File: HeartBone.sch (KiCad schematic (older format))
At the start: 42 parts, among them J1 CONN_01X05, J2 CONN_01X01, J3 CONN_01X01, J4 USB_B_Micro, SW1 PTS810_SJK_250_SMTR_LFS, SW2 PTS810_SJK_250_SMTR_LFS, SW3 SW_SPDT, U1 25LC1024T-I/SM, U2 Schmitt_Inverter_Single, U3 PIC32MX250F128B-I/SS, U4 TLV76033DBZR, U5 MCP73831-2-OT, Y1 ECS-080-18-23G-JGN-TR

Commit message: dusted off BOM
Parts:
- BT1: value Battery_Cell -> S2B-PH-SM4-TB(LF)(SN)
- D2, D3: value DIODE -> CDBU0130L
- DIS1: value SharpMem_LCD_96x96 -> 505110-1092
- J4: value USB_B_Micro -> 10118193-0001LF
- SW3: value SW_SPDT -> SSSS810701
- U2: value Schmitt_Inverter_Single -> TC7S14FU,LF
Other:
- note added: "MOLEX\n"
- note removed: "MOLEX 505110-1092\n\n"
- note removed: "SPECIFY DIODE PART NUMBER"
- note removed: "TOSHIBA TC7S14FU,LF"
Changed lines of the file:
@@
 P 8500 4050
 F 0 "DIS1" H 8850 2650 60  0000 C CNN
-F 1 "SharpMem_LCD_96x96" H 9200 3950 60  0000 C CNN
+F 1 "505110-1092" H 9000 3950 60  0000 C CNN
 F 2 "Solutions:MOLEX_505110-1092" H 8500 4050 60  0001 C CNN
 F 3 "" H 8500 4050 60  0000 C CNN
@@
 	1    0    0    -1
 $EndComp
-Text Notes 8550 2650 0    60   ~ 0
-TOSHIBA TC7S14FU,LF
 Text Notes 8650 4050 0    60   ~ 0
 Sharp has gone EOL :(
@@
 	1    0    0    -1
 $EndComp
-Text Notes 8450 5700 0    60   ~ 0
-MOLEX 505110-1092\n\n
+Text Notes 9250 4350 0    60   ~ 0
+MOLEX\n
 $Comp
 L Device:R R4
@@
 P 8650 2350
 F 0 "U2" H 8250 2150 60  0000 C CNN
-F 1 "Schmitt_Inverter_Single" H 9200 2250 60  0000 C CNN
+F 1 "TC7S14FU,LF" H 9200 2250 60  0000 C CNN
 F 2 "Solutions:SSOP-5-0.65_PITCH" H 8650 2350 60  0001 C CNN
 F 3 "" H 8650 2350 60  0000 C CNN
@@
 P 1200 1600
 F 0 "J4" H 1255 2067 50  0000 C CNN
-F 1 "USB_B_Micro" H 1255 1976 50  0000 C CNN
+F 1 "10118193-0001LF" H 1255 1976 50  0000 C CNN
 F 2 "Solutions:10118193_microUSB" H 1350 1550 50  0001 C CNN
 F 3 "~" H 1350 1550 50  0001 C CNN
@@
 P 4100 1950
 F 0 "BT1" H 4218 2046 50  0000 L CNN
-F 1 "Battery_Cell" H 4218 1955 50  0000 L CNN
+F 1 "S2B-PH-SM4-TB(LF)(SN)" H 3900 1750 50  0000 L CNN
 F 2 "Solutions:4UCON-0217-20519" V 4100 2010 50  0001 C CNN
 F 3 "~" V 4100 2010 50  0001 C CNN
@@
 U 1 1 5CE86E84
 P 5050 1950
-F 0 "C8" H 4900 2050 50  0000 L CNN
-F 1 "1uF" H 4850 1850 50  0000 L CNN
+F 0 "C8" H 5100 2050 50  0000 L CNN
+F 1 "1uF" H 5100 1850 50  0000 L CNN
 F 2 "Capacitors_SMD:C_0603" H 5050 1950 50  0001 C CNN
 F 3 "" H 5050 1950 50  0000 C CNN
@@
 P 4050 1400
 F 0 "D2" H 3900 1350 50  0000 C CNN
-F 1 "DIODE" H 4050 1275 50  0000 C CNN
+F 1 "CDBU0130L" H 4050 1275 50  0000 C CNN
 F 2 "Diodes_SMD:D_0603" H 4050 1400 50  0001 C CNN
 F 3 "~" H 4050 1400 50  0001 C CNN
@@
 P 4600 1700
 F 0 "D3" H 4450 1650 50  0000 C CNN
-F 1 "DIODE" H 4600 1575 50  0000 C CNN
+F 1 "CDBU0130L" H 4600 1575 50  0000 C CNN
 F 2 "Diodes_SMD:D_0603" H 4600 1700 50  0001 C CNN
 F 3 "~" H 4600 1700 50  0001 C CNN
@@
 	4450 1700 4100 1700
 Connection ~ 4100 1700
-Text Notes 3700 1200 0    50   ~ 0
-SPECIFY DIODE PART NUMBER
 Text Notes 2750 6700 0    50   ~ 0
 2mm MAX HEIGHT
@@
 P 6600 1700
 F 0 "SW3" H 6600 1375 50  0000 C CNN
-F 1 "SW_SPDT" H 6600 1466 50  0000 C CNN
+F 1 "SSSS810701" H 6600 1466 50  0000 C CNN
 F 2 "Solutions:SSSS810701_ALPS_SPDT" H 6600 1700 50  0001 C CNN
 F 3 "" H 6600 1700 50  0001 C CNN

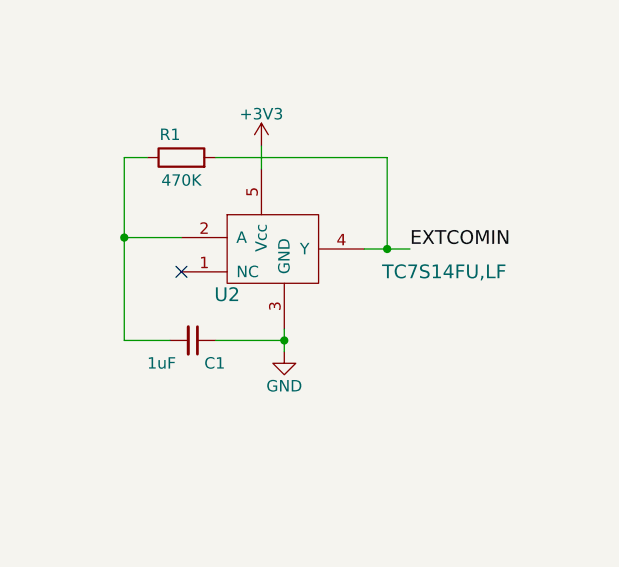
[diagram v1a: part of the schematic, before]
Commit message: UPDATED INVERTER PART NUMBER
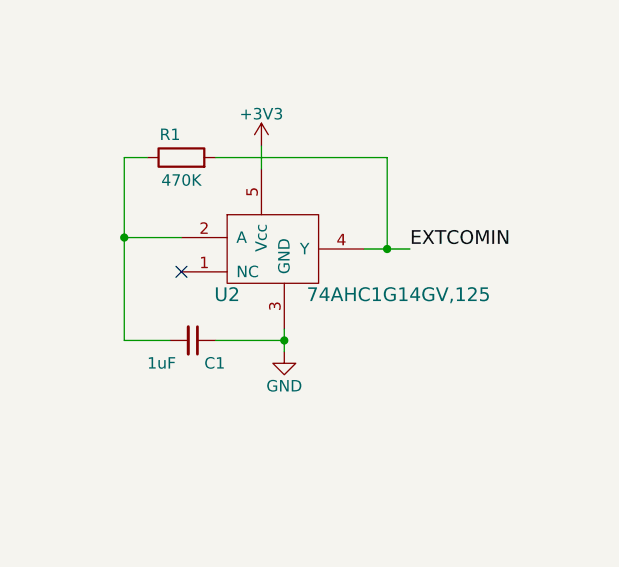
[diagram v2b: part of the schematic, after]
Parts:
- U2: value TC7S14FU,LF -> 74AHC1G14GV,125
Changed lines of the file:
@@
 EESchema Schematic File Version 4
+LIBS:HeartBone-cache
 EELAYER 26 0
 EELAYER END
@@
 P 8650 2350
 F 0 "U2" H 8250 2150 60  0000 C CNN
-F 1 "TC7S14FU,LF" H 9200 2250 60  0000 C CNN
+F 1 "74AHC1G14GV,125" H 9000 2150 60  0000 C CNN
 F 2 "Solutions:SSOP-5-0.65_PITCH" H 8650 2350 60  0001 C CNN
 F 3 "" H 8650 2350 60  0000 C CNN
